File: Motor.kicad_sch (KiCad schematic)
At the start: 12 parts, among them J2 Encoder, M1 NEMA8, U10 AM26C32IDR

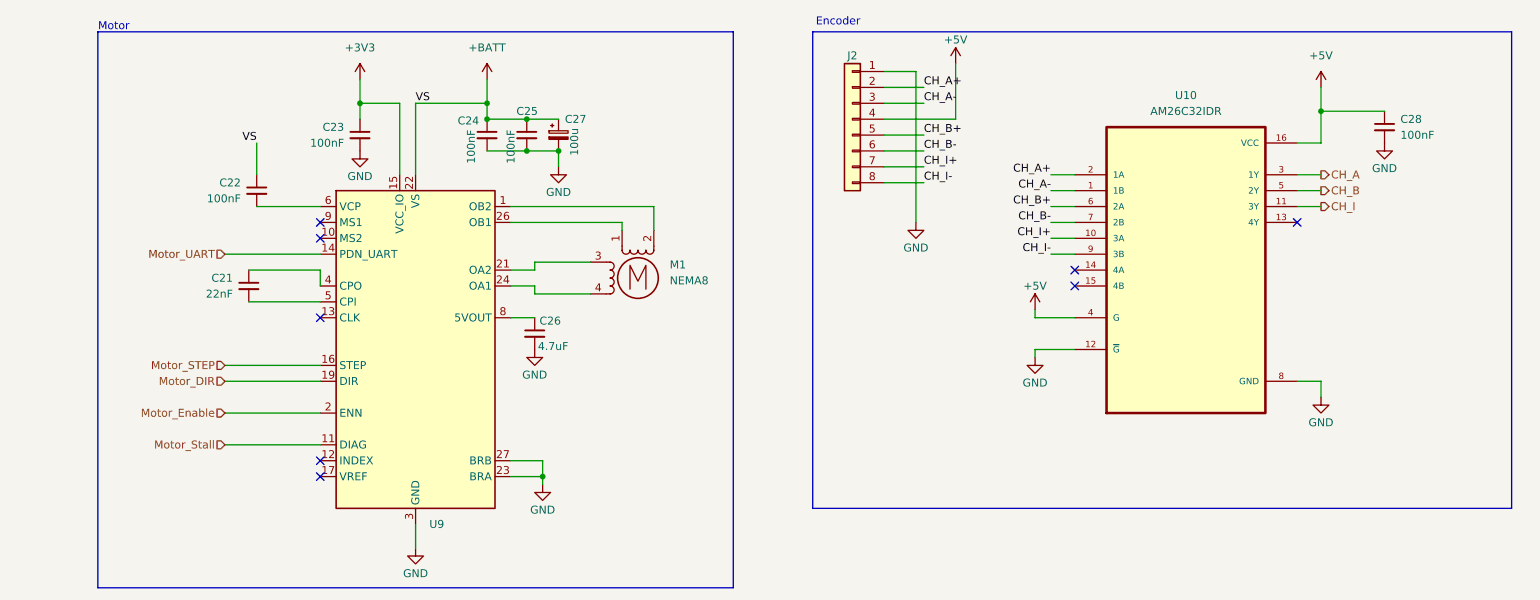
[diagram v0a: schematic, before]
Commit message: Schematic updated for V2.0, updating PCB now
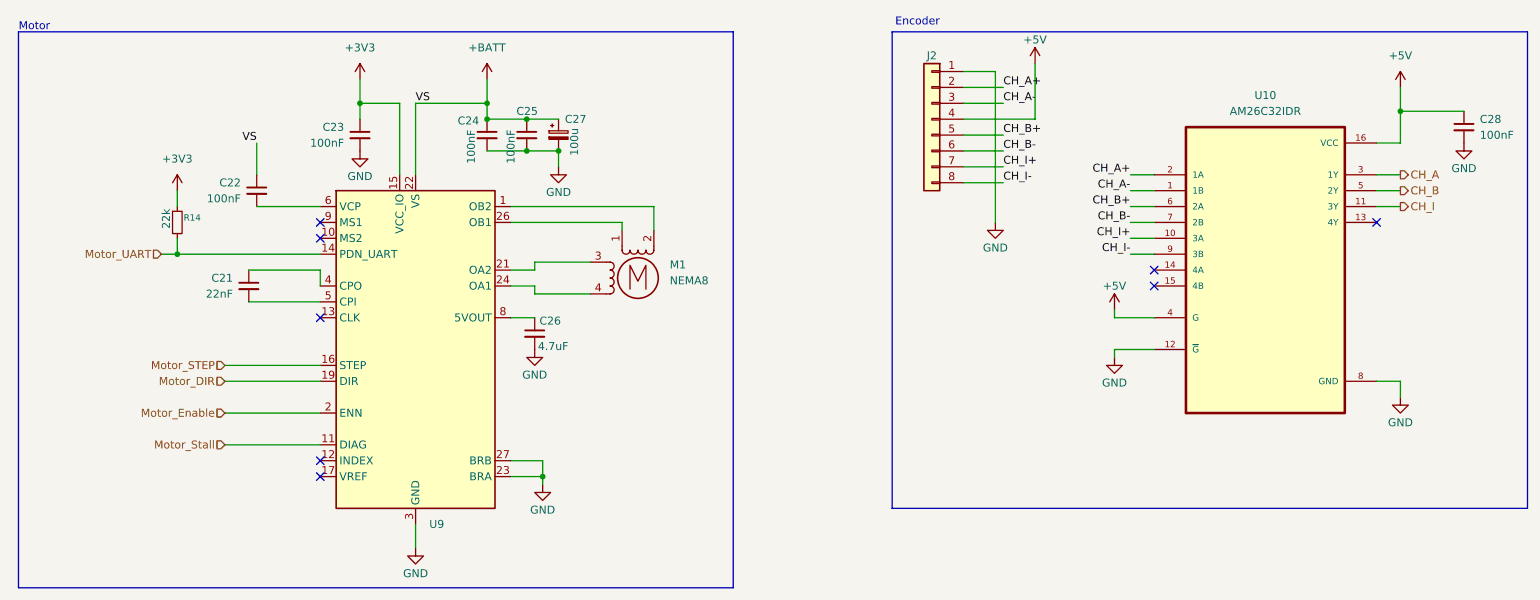
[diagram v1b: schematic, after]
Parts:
- added R14: 22k, Resistor_SMD:R_0402_1005Metric, symbol Device:R_Small
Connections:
- net +3V3: now also R14.1
- net Motor_UART: now also R14.2
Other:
- moved on the sheet: C28, J2, U10
